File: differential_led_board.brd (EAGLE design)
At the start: 100 x 50 mm, 26 parts, among them IC1 TJA1057

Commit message: Cleaned up output and differential driver boards; added basic differential receiver board
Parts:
- removed LED2: (no value), led:CHIPLED_1206
- added C10, C12, C13, C18, C19, C9: 100nF, rcl:C0805
- added C11: 470µF, rcl:UD-8X10_NICHICON
- added C21: 4.7µF, rcl:C0805
- added H4: MOUNT-HOLE2.8, holes:2,8
- added IC2: TJA1057, lichtenstein_onion:SOIC8
- added IC3: AT25SF041, lichtenstein_onion:SOIC8
- added IC4: LMS33460, lichtenstein_onion:SC70-5L
- added IC5: SN75175SOP-16, lichtenstein_onion:SOP-16
- added IC6: STM32F042F, lichtenstein_onion:TSSOP20
- added IC7: (no value), lichtenstein_onion:SOT26
- added IC8, IC9: (no value), lichtenstein_onion:SOT457R_PHILIPS
- added J1: 1792863, lichtenstein_onion:1792863
- added LED3, LED5, LED6: (no value), led:CHIPLED_1206
- added Q1: 8MHz, crystal:HC49UP
- added R10, R7: 330R, rcl:M0805
- added R8, R9: 680R, rcl:M0805
- C2: value 100nF -> 33pF
- C3: value 47µF -> 100nF; device rcl:CT6032 -> rcl:C0805
- C4: value 10µF -> 33pF; device rcl:SMC_B -> rcl:C0805
- C5: value 4.7nF -> 100nF
- C6: value 4.7nF -> 47µF; device rcl:C0805 -> rcl:CT6032
- IC1: value TJA1057 -> LD1117S33; device lichtenstein_onion:SOIC8 -> lichtenstein_onion:SOT223
- R1: value 1k2 -> 100R; device rcl:M0805 -> rcl:M1206
- R3: value 49R9 -> 1k; device rcl:M1206 -> rcl:M0805
- R4: value 49R9 -> 100R
- R5, R6: value 49R9 -> 10k; device rcl:M1206 -> rcl:M0805
- SV2: value SS-51000-003 -> 1792889; device lichtenstein_onion:SS-51000-003 -> lichtenstein_onion:1792889
- SV3: value (none) -> 1792889; device con-lstb:MA12-2 -> lichtenstein_onion:1792889
- SV4: value SS-51000-003 -> (none); device lichtenstein_onion:SS-51000-003 -> con-lstb:MA03-1
- SV5: value SS-51000-003 -> CORTEX_DEBUG_PTH; device lichtenstein_onion:SS-51000-003 -> lichtenstein_onion:2X5-PTH-1.27MM
- moved SV3 159.3 mm to (7.37, -108.5), turned to 0 degrees
- moved H3 104.2 mm to (16.0, 112.0)
- moved SV2 102.0 mm to (7.37, -96.0)
- moved C6 89.2 mm to (22.4, 88.9), turned to 90 degrees
- moved LED1 83.8 mm to (9.65, 80.5), turned to 180 degrees
- moved R2 82.2 mm to (9.65, 85.6), turned to 270 degrees
- moved H2 77.4 mm to (55.9, 112.0)
- moved R3 76.0 mm to (9.65, 90.9), turned to 90 degrees
- moved R6 75.6 mm to (1.78, -50.0)
- moved C3 71.6 mm to (16.3, 81.3), turned to 270 degrees
- moved R5 68.6 mm to (1.78, -43.7), turned to 0 degrees
- moved C1 66.0 mm to (91.9, -18.3), flipped to the top, turned to 0 degrees
- moved H1 65.4 mm to (55.9, 5.08)
- moved C8 62.6 mm to (8.38, -23.1), turned to 0 degrees
- moved C7 62.5 mm to (2.03, -23.1), turned to 0 degrees
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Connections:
- removed net CANH_1: SV1.8, SV2.6
- removed net CANH_2: SV2.8, SV4.6
- removed net CANH_3: SV4.8, SV5.6
- removed net CANH_4: R5.1, SV5.8
- removed net CANL_1: SV1.7, SV2.5
- removed net CANL_2: SV2.7, SV4.5
- removed net CANL_3: SV4.7, SV5.5
- removed net CANL_4: R6.2, SV5.7
- removed net N$13: LED1.A, R1.2
- removed net N$14: LED2.A, R2.2
- removed net OUT2_N: SV2.1, SV3.12
- removed net OUT2_P: SV2.2, SV3.10
- removed net OUT3_N: SV2.3, SV3.8
- removed net OUT3_P: SV2.4, SV3.6
- removed net OUT4_N: SV3.7, SV4.3
- removed net OUT4_P: SV3.5, SV4.4
- removed net OUT5_N: SV3.11, SV4.1
- removed net OUT5_P: SV3.9, SV4.2
- removed net OUT6_N: SV3.15, SV5.3
- removed net OUT6_P: SV3.13, SV5.4
- removed net OUT7_N: SV3.19, SV5.1
- removed net OUT7_P: SV3.17, SV5.2
- new net !RST: IC4.4, IC6.4, SV5.10
- new net !SPI_CS: IC3.1, IC6.10
- new net ADC_CURRENT: IC6.7
- new net ADC_VCC: IC6.6
- new net CORTEX_OSC1: C4.2, IC6.2, Q1.2
- new net CORTEX_OSC2: C2.2, IC6.3, Q1.1
- new net CORTEX_SWCLK: IC6.20, R9.1, SV5.4
- new net CORTEX_SWDIO: IC6.19, R8.1, SV5.2
- new net LEDOUT0: IC5.3, IC8.3
- new net LEDOUT1: IC5.5, IC9.3
- new net LEDOUT_TEST: IC6.14, IC7.3
- new net LEDOUT_TEST_5V: IC7.4, IC8.1, IC9.1
- new net N$3: R10.1, SV3.1
- new net N$4: LED5.A, R8.2
- new net N$5: LED6.A, R9.2
- new net N$6: R7.1, SV2.1
- new net OUT0: IC8.4, R7.2
- new net OUT0_MUX: IC6.9, IC8.6, R6.2, SV4.3
- new net OUT1: IC9.4, R10.2
- new net OUT1_MUX: IC6.1, IC9.6, R5.2
- new net SPI_MISO: IC3.2, IC6.12
- new net SPI_MOSI: IC3.5, IC5.4, IC6.13
- new net SPI_SCK: IC3.6, IC6.11
- new net UART_TX: IC6.8, SV4.2
- net +3V3: now also C1.1, C13.1, C18.1, C19.1, C21.1, C3.1, C6.+, IC1.2, IC1.4, IC2.5, IC3.3, IC3.7, IC3.8, IC4.5, IC6.16, IC6.5, IC7.1, IC7.5, SV5.1; no longer C2.1, C4.+, IC1.5, SV3.2
- net +5V: now also C10.1, C11.+, C12.1, C5.1, C9.1, IC2.3, IC5.16, IC7.6, IC8.5, IC9.5, J1.2, R3.1, SV2.4; no longer C1.1, C3.+, R1.1
- net CANH: now also IC2.7, SV1.8; no longer IC1.7, R3.2
- net CANL: now also IC2.6, SV1.7; no longer IC1.6, R4.1
- net CAN_RX: now also IC2.4, IC6.17; no longer IC1.4, SV3.23
- net CAN_TX: now also IC2.1, IC6.18; no longer IC1.1, SV3.24
- net GND: now also C10.2, C11.-, C12.2, C13.2, C18.2, C19.2, C2.1, C21.2, C3.2, C4.1, C6.-, C9.2, IC1.1, IC2.2, IC2.8, IC3.4, IC4.2, IC4.3, IC5.12, IC5.8, IC6.15, IC7.2, IC8.2, IC9.2, J1.1, LED3.C, LED5.C, LED6.C, R5.1, R6.1, SV2.2, SV2.3, SV3.2, SV4.1, SV5.3, SV5.5, SV5.9; no longer C2.2, C3.-, C4.-, C6.2, IC1.2, IC1.8, LED2.C, SV3.1, SV3.21, SV3.22
- net N$1: now also LED1.A, R2.2; no longer C5.1, R3.1, R4.2
- net N$2: now also LED3.A, R3.2; no longer C6.1, R5.2, R6.1
- net OUT0_N: now also IC5.1, R1.1; no longer SV3.20
- net OUT0_P: now also IC5.2, R1.2; no longer SV3.18
- net OUT1_N: now also IC5.7, R4.1; no longer SV3.16
- net OUT1_P: now also IC5.6, R4.2; no longer SV3.14
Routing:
- net OUT2_N: track 62.0 -> 0.00 mm
- net OUT2_P: track 61.0 -> 0.00 mm
- net OUT3_N: track 57.9 -> 0.00 mm
- net OUT3_P: track 57.4 -> 0.00 mm
- net +5V: track 87.4 -> 31.2 mm, vias 1 -> 0
- net CANL_2: track 53.5 -> 0.00 mm
- net CANH_2: track 52.7 -> 0.00 mm
- net OUT6_N: track 51.5 -> 0.00 mm
- net OUT6_P: track 51.0 -> 0.00 mm
- net OUT7_P: track 50.0 -> 0.00 mm
- net OUT7_N: track 49.5 -> 0.00 mm
- net +3V3: track 68.4 -> 23.1 mm
- net OUT0_N: track 45.1 -> 0.00 mm
- net OUT0_P: track 44.2 -> 0.00 mm
- net CANH_4: track 42.0 -> 0.00 mm
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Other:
- board size 100 x 50 mm -> 72 x 117 mm
- board text added: "+3V3 Good"
- board text added: "+5V Good"
- board text added: "+5V In"
- board text added: "Lichtenstein Differential Output © 2018 Tristan Seifert"
- board text removed: "5V Good 3V3 Good"
- board text removed: "CAN Out CAN Return"
- board text removed: "Ch0 Ch1 Ch2 Ch3"
- board text removed: "Ch4 Ch5 Ch6 Ch7"
- board text removed: "Lichtenstein Differential Output Board with CAN (c) 2018 Tristan Seifert"

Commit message: Finished output stage of differential LED board; started routing CANnabus controller/power sections
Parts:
- added R11, R12: 1k, rcl:M0805
- moved R10 172.7 mm to (44.5, 42.7), turned to 90 degrees
- moved R7 160.7 mm to (12.7, 42.7), turned to 90 degrees
- moved C10 147.9 mm to (76.5, 52.1)
- moved C12 147.9 mm to (76.5, 45.7)
- moved C13 147.9 mm to (76.5, 39.4)
- moved C9 147.9 mm to (76.5, 58.4)
- moved R5 147.9 mm to (80.0, 81.8)
- moved R6 147.9 mm to (80.0, 75.4)
- moved C18 140.1 mm to (43.2, 101.6), flipped to the bottom, turned to 90 degrees
- moved SV3 139.9 mm to (52.1, 24.1)
- moved C7 136.2 mm to (56.1, 101.9), turned to 90 degrees
- moved C8 133.1 mm to (54.1, 101.9), turned to 90 degrees
- moved C19 129.8 mm to (43.2, 89.7), turned to 270 degrees
- moved C21 127.0 mm to (36.6, 96.0), turned to 180 degrees
- moved IC4 126.5 mm to (37.8, 82.0)
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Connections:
- removed net ADC_VCC: IC6.6
- new net ADC_VIN: IC6.6, R11.1, R12.2
- net +5V: now also R11.2
- net GND: now also R12.1
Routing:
- net +5V: track 31.2 -> 242.4 mm, vias 0 -> 2
- net +3V3: track 23.1 -> 87.7 mm, vias 0 -> 1
- net UART_TX: track 0.00 -> 27.8 mm, vias 0 -> 1
- net OUT0_MUX: track 0.00 -> 26.7 mm, vias 0 -> 1
- net CANL: track 0.00 -> 22.0 mm
- net CANH: track 0.00 -> 20.9 mm
- net CORTEX_SWCLK: track 0.00 -> 20.1 mm, vias 0 -> 1
- net !RST: track 0.00 -> 19.6 mm, vias 0 -> 1
- net CORTEX_SWDIO: track 0.00 -> 18.8 mm, vias 0 -> 1
- net N$6: track 0.00 -> 17.7 mm
- net N$3: track 0.00 -> 17.7 mm
- net CORTEX_OSC2: track 0.00 -> 14.9 mm
- net CORTEX_OSC1: track 0.00 -> 14.6 mm
- net SPI_MISO: track 0.00 -> 13.5 mm, vias 0 -> 2
- net !SPI_CS: track 0.00 -> 13.3 mm
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
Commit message: Added LT6100 to measure current (todo: add shunt connections)
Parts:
- added C14, C16: 100nF, rcl:C0805
- added C15: 4.7µF, rcl:C0805
- added IC10: (no value), lichtenstein_onion:MSOP8
- moved R6 67.9 mm to (17.5, 48.8), turned to 270 degrees
- moved C10 58.4 mm to (18.5, 44.7)
- moved C13 49.7 mm to (31.2, 59.9)
- moved C12 48.1 mm to (31.2, 62.2)
- moved R5 45.1 mm to (49.3, 48.8), turned to 270 degrees
- moved C9 29.5 mm to (50.3, 44.7)
- moved C5 27.8 mm to (50.0, 59.9), turned to 45 degrees
- moved IC5 11.6 mm to (47.2, 66.5), turned to 135 degrees
- moved C7 10.4 mm to (55.9, 91.4), turned to 180 degrees
- moved IC4 0.57 mm to (38.4, 81.8)
- moved IC7 0.25 mm to (27.2, 63.5)
- moved SV4 0.25 mm to (32.3, 85.3)
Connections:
- new net N$7: C16.2, IC10.3
- new net SHUNT+: IC10.8
- new net SHUNT-: IC10.1
- net +3V3: now also C14.1, C15.1, IC10.2
- net ADC_CURRENT: now also IC10.5
- net GND: now also C14.2, C15.2, C16.1, IC10.4, IC10.7
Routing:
- net +5V: track 242.4 -> 338.9 mm, vias 2 -> 4
- net +3V3: track 87.7 -> 147.7 mm, vias 1 -> 2
- net LEDOUT0: track 0.00 -> 57.4 mm
- net OUT1_MUX: track 0.00 -> 56.2 mm, vias 0 -> 2
- net OUT0_MUX: track 26.7 -> 80.9 mm, vias 1 -> 3
- net ADC_CURRENT: track 0.00 -> 48.3 mm, vias 0 -> 2
- net LEDOUT_TEST_5V: track 0.00 -> 46.9 mm, vias 0 -> 3
- net SPI_MOSI: track 8.97 -> 40.7 mm, vias 0 -> 2
- net LEDOUT_TEST: track 12.2 -> 39.9 mm
- net LEDOUT1: track 0.00 -> 22.7 mm, vias 0 -> 2
- net OUT1_P: track 5.24 -> 25.0 mm, vias 0 -> 1
- net OUT1_N: track 5.39 -> 22.5 mm, vias 0 -> 1
- net OUT0_P: track 5.13 -> 18.2 mm, vias 0 -> 1
- net OUT0_N: track 5.49 -> 16.2 mm, vias 0 -> 1
- net N$7: track 0.00 -> 3.60 mm
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
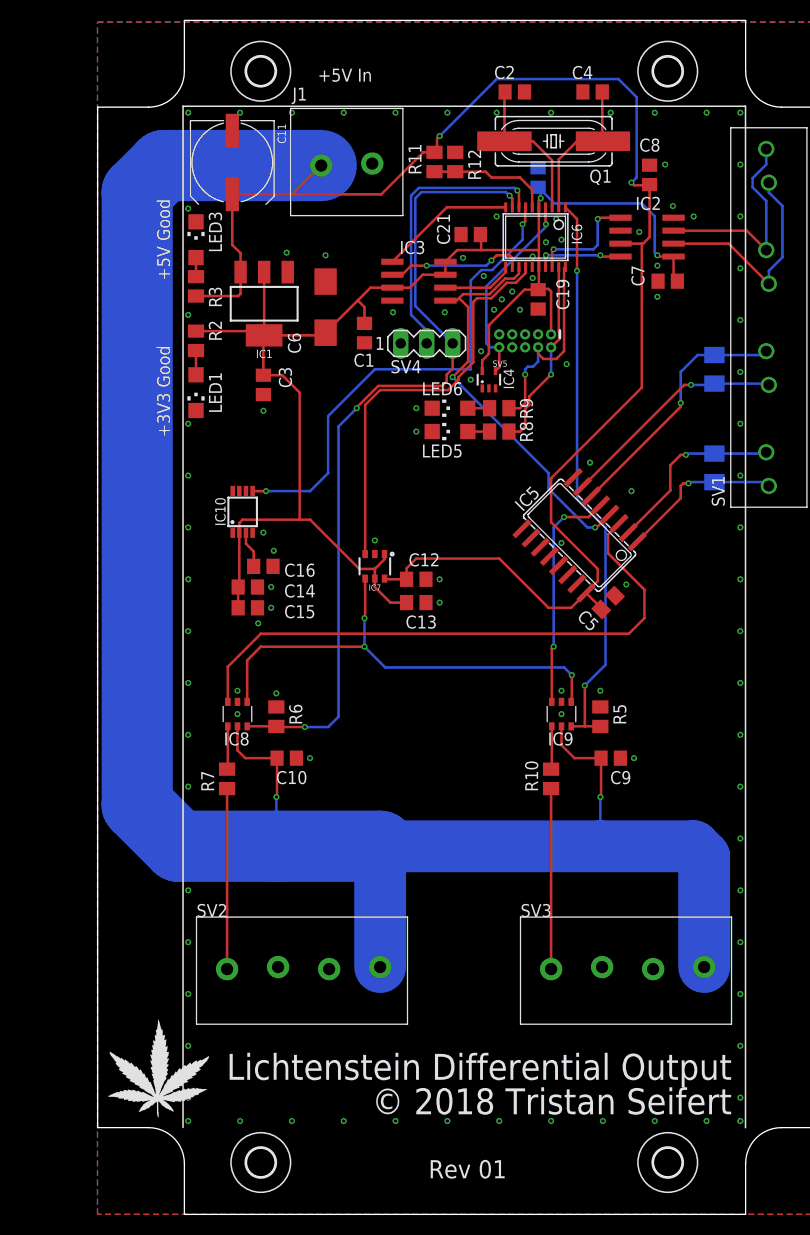
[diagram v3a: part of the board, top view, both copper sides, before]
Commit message: finished routing LED board; substituted a few components and fixed missing level translation
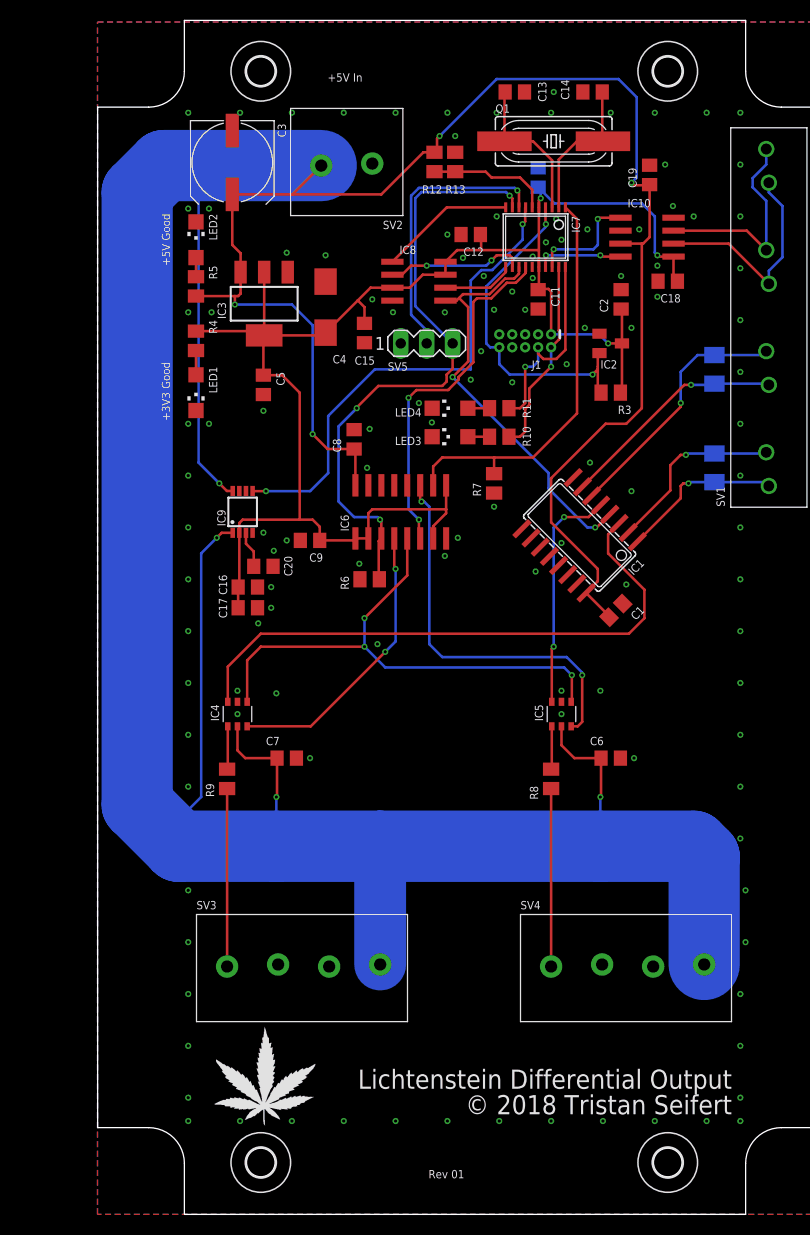
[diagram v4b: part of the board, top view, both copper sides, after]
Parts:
- removed C21: 4.7µF, rcl:C0805
- removed LED5: (no value), led:CHIPLED_1206
- added C17: 4.7µF, rcl:C0805
- added C20: 100nF, rcl:C0805
- added LED2: GRN, led:CHIPLED_1206
- added R13: 1k, rcl:M0805
- C11: value 470µF -> 100nF; device rcl:UD-8X10_NICHICON -> rcl:C0805
- C12: value 100nF -> 4.7µF
- C13, C14: value 100nF -> 33pF
- C15: value 4.7µF -> 100nF
- C2: value 33pF -> 100nF
- C3: value 100nF -> 470µF; device rcl:C0805 -> rcl:UD-8X10_NICHICON
- C4: value 33pF -> 47µF; device rcl:C0805 -> rcl:CT6032
- C6: value 47µF -> 100nF; device rcl:CT6032 -> rcl:C0805
- IC1: value LD1117S33 -> SN75175SOP-16; device lichtenstein_onion:SOT223 -> lichtenstein_onion:SOP-16
- IC10: value (none) -> TJA1057; device lichtenstein_onion:MSOP8 -> lichtenstein_onion:SOIC8
- IC2: value TJA1057 -> (none); device lichtenstein_onion:SOIC8 -> lichtenstein_onion:SOT23
- IC3: value AT25SF041 -> LD1117S33; device lichtenstein_onion:SOIC8 -> lichtenstein_onion:SOT223
- IC4: value LMS33460 -> 74LVC1G157; device lichtenstein_onion:SC70-5L -> lichtenstein_onion:SOT457R_PHILIPS
- IC5: value SN75175SOP-16 -> 74LVC1G157; device lichtenstein_onion:SOP-16 -> lichtenstein_onion:SOT457R_PHILIPS
- IC6: value STM32F042F -> CD40109B; device lichtenstein_onion:TSSOP20 -> lichtenstein_onion:SO16
- IC7: value (none) -> STM32F042F; device lichtenstein_onion:SOT26 -> lichtenstein_onion:TSSOP20
- IC8: value (none) -> AT25SF041; device lichtenstein_onion:SOT457R_PHILIPS -> lichtenstein_onion:SOIC8
- IC9: value (none) -> LT6100; device lichtenstein_onion:SOT457R_PHILIPS -> lichtenstein_onion:MSOP8
- J1: value 1792863 -> CORTEX_DEBUG_PTH; device lichtenstein_onion:1792863 -> lichtenstein_onion:2X5-PTH-1.27MM
- LED1, LED3, LED4: value (none) -> GRN
- R10: value 330R -> 680R
- R11: value 1k -> 680R
- R2: value 680R -> 100R; device rcl:M0805 -> rcl:M1206
- R3: value 1k -> 10k
- R4: value 100R -> 680R; device rcl:M1206 -> rcl:M0805
- R5: value 10k -> 1k
- R7: value 330R -> 10k
- R8, R9: value 680R -> 330R
- SV2: value 1792889 -> 1792863; device lichtenstein_onion:1792889 -> lichtenstein_onion:1792863
- SV4: value (none) -> 1792889; device con-lstb:MA03-1 -> lichtenstein_onion:1792889
- SV5: value CORTEX_DEBUG_PTH -> (none); device lichtenstein_onion:2X5-PTH-1.27MM -> con-lstb:MA03-1
- moved H1 114.1 mm to (16.0, 112.0)
- moved H2 114.1 mm to (16.0, 5.08)
- moved H3 114.1 mm to (55.9, 5.08)
- moved H4 114.1 mm to (55.9, 112.0)
- moved SV2 79.0 mm to (26.9, 102.9), turned to 180 degrees
- moved SV4 64.1 mm to (52.1, 24.4)
- moved C10 62.0 mm to (43.2, 101.6), flipped to the bottom, turned to 90 degrees
- moved C7 59.8 mm to (18.5, 44.7), turned to 0 degrees
- moved C14 59.1 mm to (48.5, 110.0)
- moved R5 57.9 mm to (9.65, 90.9), turned to 90 degrees
- moved C6 52.3 mm to (50.3, 44.7), turned to 0 degrees
- moved C13 51.0 mm to (40.9, 110.0), turned to 180 degrees
- moved R2 50.9 mm to (60.5, 82.8), flipped to the bottom, turned to 90 degrees
- moved R4 50.9 mm to (9.65, 85.6), flipped to the top, turned to 270 degrees
- moved IC10 47.9 mm to (53.8, 95.8), turned to 270 degrees
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- renumbered LED6 to LED4
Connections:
- new net OUT0_MUX_5V: IC4.6, IC6.4
- new net OUT1_MUX_5V: IC5.6, IC6.11
- net !RST: now also IC2.2, IC7.4, J1.10, R3.1; no longer IC4.4, IC6.4, SV5.10
- net !SPI_CS: now also IC7.10, IC8.1; no longer IC3.1, IC6.10
- net +3V3: now also C10.1, C11.1, C12.1, C16.1, C17.1, C2.1, C4.+, C5.1, C9.1, IC10.5, IC2.3, IC3.2, IC3.4, IC6.1, IC6.2, IC6.7, IC6.9, IC7.16, IC8.3, IC8.7, IC8.8, IC9.2, J1.1, R3.2, R4.1; no longer C1.1, C13.1, C14.1, C19.1, C21.1, C3.1, C6.+, C7.1, IC1.2, IC1.4, IC10.2, IC2.5, IC3.3, IC3.7, IC3.8, IC4.5, IC6.16, IC6.5, IC7.1, R2.1, SV5.1
- net +5V: now also C1.1, C19.1, C3.+, C6.1, C7.1, IC1.16, IC10.3, IC3.3, IC4.5, IC5.5, IC6.16, R12.2, R5.1, SV2.2, SV4.4; no longer C10.1, C11.+, C12.1, C5.1, C9.1, IC1.3, IC2.3, IC5.16, IC7.6, IC8.5, IC9.5, J1.2, R11.2, R3.1, SV2.4
- net ADC_CURRENT: now also IC7.7, IC9.5; no longer IC10.5, IC6.7
- net ADC_VIN: now also IC7.6, R12.1, R13.2; no longer IC6.6, R11.1, R12.2
- net CANH: now also IC10.7; no longer IC2.7
- net CANL: now also IC10.6; no longer IC2.6
- net CAN_RX: now also IC10.4, IC7.17; no longer IC2.4, IC6.17
- net CAN_TX: now also IC10.1, IC7.18; no longer IC2.1, IC6.18
- net CORTEX_OSC1: now also C14.2, IC7.2; no longer C4.2, IC6.2
- net CORTEX_OSC2: now also C13.2, IC7.3; no longer C2.2, IC6.3
- net CORTEX_SWCLK: now also IC7.20, J1.4, R11.1; no longer IC6.20, R9.1, SV5.4
- net CORTEX_SWDIO: now also IC7.19, J1.2, R10.1; no longer IC6.19, R8.1, SV5.2
- net GND: now also C11.2, C13.1, C14.1, C16.2, C17.2, C2.2, C20.1, C3.-, C4.-, C6.2, IC1.12, IC1.8, IC10.2, IC10.8, IC2.1, IC3.1, IC5.2, IC6.8, IC7.15, IC8.4, IC9.4, IC9.7, J1.3, J1.5, J1.9, LED2.C, R13.1, R7.1, SV2.1, SV4.2, SV4.3, SV5.1; no longer C11.-, C13.2, C14.2, C16.1, C2.1, C21.2, C3.2, C4.1, C6.-, IC1.1, IC10.4, IC10.7, IC2.2, IC2.8, IC3.4, IC4.3, IC5.12, IC5.8, IC7.2, IC8.2, IC9.2, J1.1, LED5.C, R12.1, R5.1, SV2.2, SV2.3, SV4.1, SV5.3, SV5.5, SV5.9
- net LEDOUT0: now also IC1.3, IC4.3; no longer IC5.3, IC8.3
- net LEDOUT1: now also IC1.5, IC5.3; no longer IC5.5, IC9.3
- net LEDOUT_TEST: now also IC6.6, IC7.14; no longer IC6.14, IC7.3
- net LEDOUT_TEST_5V: now also IC4.1, IC5.1, IC6.5; no longer IC7.4, IC8.1, IC9.1
- net N$1: now also R4.2; no longer R2.2
- net N$2: now also LED2.A, R5.2; no longer LED3.A, R3.2
- net N$3: now also R8.1, SV4.1; no longer R10.1, SV3.1
- net N$4: now also LED3.A, R10.2; no longer LED5.A, R8.2
- net N$5: now also R11.2; no longer R9.2
- net N$6: now also R9.1, SV3.1; no longer R7.1, SV2.1
- net N$7: now also C20.2, IC9.3; no longer C16.2, IC10.3
- net OUT0: now also IC4.4, R9.2; no longer IC8.4, R7.2
- net OUT0_MUX: now also IC6.3, IC7.9, SV5.3; no longer IC6.9, IC8.6, SV4.3
- net OUT0_N: now also IC1.1; no longer IC5.1
- net OUT0_P: now also IC1.2; no longer IC5.2
- net OUT1: now also IC5.4, R8.2; no longer IC9.4, R10.2
- net OUT1_MUX: now also IC6.10, IC7.1, R7.2; no longer IC6.1, IC9.6, R5.2
- net OUT1_N: now also IC1.7, R2.1; no longer IC5.7, R4.1
- net OUT1_P: now also IC1.6, R2.2; no longer IC5.6, R4.2
- net SHUNT+: now also IC9.8; no longer IC10.8
- net SHUNT-: now also IC9.1; no longer IC10.1
- net SPI_MISO: now also IC7.12, IC8.2; no longer IC3.2, IC6.12
- net SPI_MOSI: now also IC1.4, IC7.13, IC8.5; no longer IC3.5, IC5.4, IC6.13
- net SPI_SCK: now also IC7.11, IC8.6; no longer IC3.6, IC6.11
- net UART_TX: now also IC7.8, SV5.2; no longer IC6.8, SV4.2
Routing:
- net OUT1_MUX_5V: track 0.00 -> 38.3 mm, vias 0 -> 2
- net SHUNT+: track 0.00 -> 36.8 mm, vias 0 -> 1
- net SHUNT-: track 0.00 -> 36.1 mm, vias 0 -> 1
- net OUT0_MUX_5V: track 0.00 -> 28.1 mm, vias 0 -> 2
- net OUT0_MUX: track 80.9 -> 61.4 mm
- net OUT1_MUX: track 56.2 -> 40.4 mm, vias 2 -> 0
- net !RST: track 19.7 -> 33.2 mm, vias 1 -> 2
- net +3V3: track 147.7 -> 159.8 mm, vias 2 -> 3
- net +5V: track 338.9 -> 345.1 mm, vias 4 -> 6
- net LEDOUT_TEST_5V: track 46.9 -> 52.6 mm
- net LEDOUT_TEST: track 39.9 -> 35.0 mm, vias 0 -> 2
- net CORTEX_SWDIO: track 18.8 -> 19.3 mm
